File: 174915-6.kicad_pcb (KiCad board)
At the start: 2 copper layers, 178 x 36.6 mm, 43 parts, among them P1 CONN_3, P10 CONN_1, P11 CONN_1, P12 CONN_1, P13 CONN_3, P14 CONN_3, P15 CONN_1, P16 CONN_1, P17 CONN_1, P18 CONN_1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

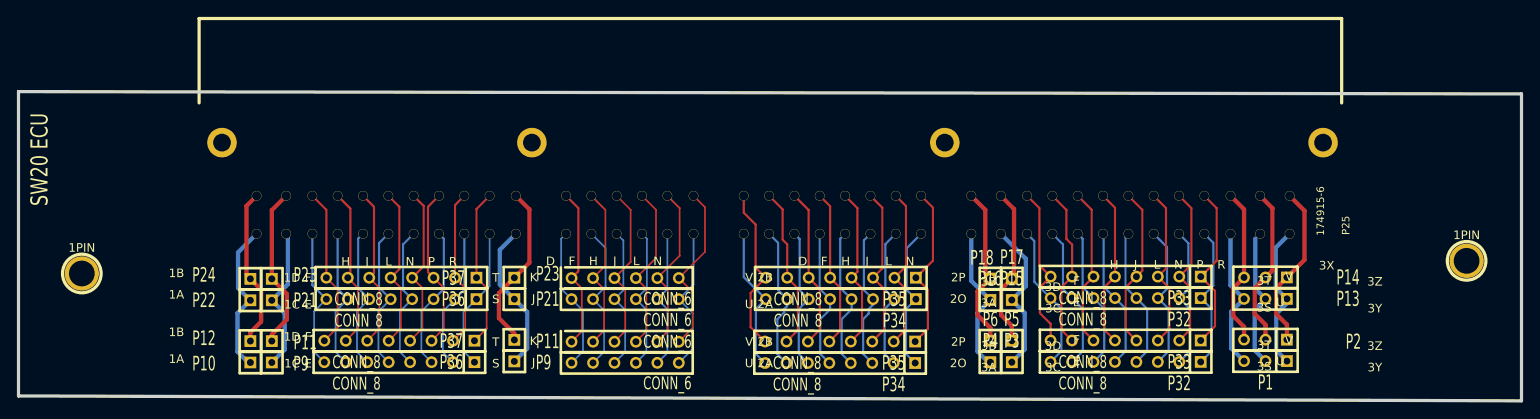
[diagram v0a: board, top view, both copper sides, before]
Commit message: adjusted width and hole position
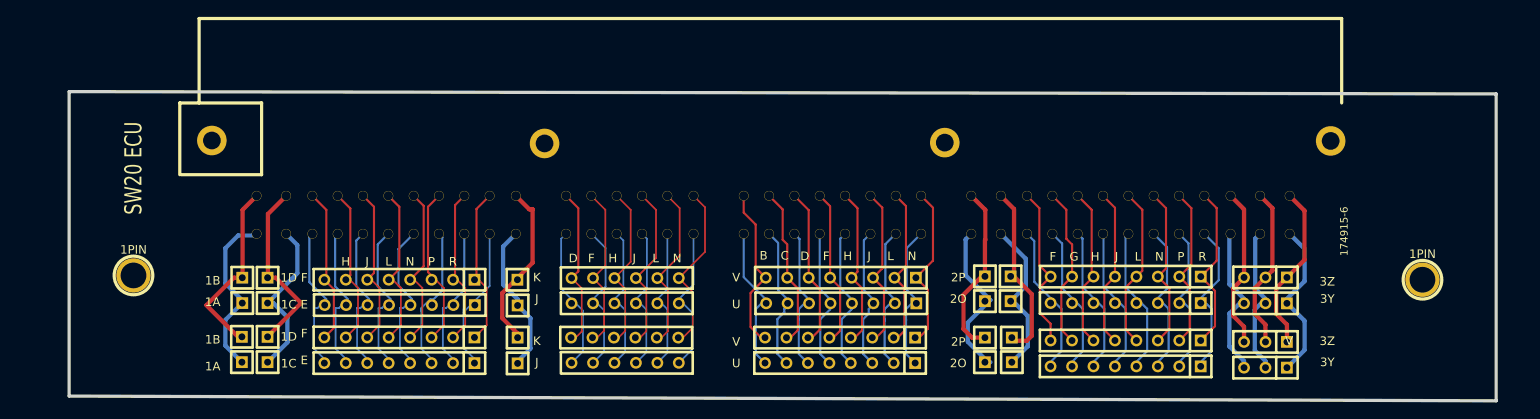
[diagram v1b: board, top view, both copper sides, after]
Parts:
- moved 1PIN 6.12 mm to (55.1, 62.2)
- moved 1PIN 5.69 mm to (207.8, 62.7)
- moved P12 1.12 mm to (68.0, 69.5)
- moved P22 1.01 mm to (68.0, 65.5)
- moved P10 1.00 mm to (68.0, 72.5)
- moved P24 0.97 mm to (68.0, 62.5)
- moved P21 0.84 mm to (100.6, 65.8)
- moved P1 0.78 mm to (189.2, 73.2)
- moved P6 0.74 mm to (156.0, 69.6)
- moved P36 0.72 mm to (86.7, 65.7)
- moved P11 0.71 mm to (71.0, 69.5)
- moved P18 0.69 mm to (156.0, 62.3)
- moved P16 0.66 mm to (156.0, 65.3)
- moved P4 0.64 mm to (156.0, 72.5)
- moved P21 0.60 mm to (71.0, 65.5)
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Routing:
- net thick: track 111.7 -> 121.4 mm
- net N-000009: track 19.0 -> 21.4 mm
- net N-000001: track 17.4 -> 19.2 mm
- net N-000008: track 17.6 -> 19.1 mm
- net N-000010: track 19.4 -> 20.7 mm
- net N-000003: track 17.0 -> 18.1 mm
- net N-000002: track 16.9 -> 17.6 mm
- net N-000064: track 19.1 -> 18.4 mm
- net N-000017: track 17.3 -> 17.8 mm
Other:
- board size 178 x 36.6 mm -> 169 x 36.6 mm
- board text added: "B"
- board text added: "C"
- board text added: "G"
- board text removed: "2A"
- board text removed: "2B"
- board text removed: "3A"
- board text removed: "3B"
- board text removed: "3C"
- board text removed: "3D"
- board text removed: "3S"
- board text removed: "3T"
- board text removed: "3X"
- board text removed: "S"
- board text removed: "T"
